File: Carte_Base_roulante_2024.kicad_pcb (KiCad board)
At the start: 2 copper layers, 62 x 80 mm, 69 parts, among them J11 ENCA, J4 ENCB, J5 ENCC, Q2 IRF7424, U1 STM32G484RETx

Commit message: Routage Terminé git status !
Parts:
- moved C2 0.19 mm to (213.2, 78.8)
- moved C4 0.19 mm to (213.2, 103.6)
- moved TP_GND1 0.13 mm to (177.3, 82.5)
- moved Transfo5->3.3 0.13 mm to (168.4, 127.2)
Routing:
- net GND: track 0.00 -> 120.9 mm, vias 0 -> 84
- net Net-(MOT2-Pin_1): track 0.00 -> 9.44 mm
- net /BOOT 0: track 16.5 -> 17.4 mm
- net IMU_INT1: track 7.10 -> 7.82 mm
- net +BATT: vias 9 -> 14
- added copper zone on B.Cu, net GND
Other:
- board size 62 x 80 mm -> 66 x 84 mm

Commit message: j'ai pas fait Ctrl S ...
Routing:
- net Enc2_B: track 23.0 -> 22.3 mm
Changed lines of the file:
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@@
   (segment (start 183.136 108.672) (end 183.136 109.757226) (width 0.3) (layer "F.Cu") (net 8))
   (segment (start 172.847 116.205) (end 176.022 113.03) (width 0.4) (layer "F.Cu") (net 8))
-  (segment (start 183.136 109.757226) (end 182.641613 110.251613) (width 0.3) (layer "F.Cu") (net 8))
   (segment (start 179.933938 113.03) (end 183.171356 109.792582) (width 0.4) (layer "F.Cu") (net 8))
   (segment (start 164.592 116.205) (end 172.847 116.205) (width 0.4) (layer "F.Cu") (net 8))
@@
   (segment (start 181.4025 93.7725) (end 180.34 93.7725) (width 0.3) (layer "B.Cu") (net 26))
   (segment (start 184.15 99.06) (end 183.515 98.425) (width 0.3) (layer "B.Cu") (net 26))
-  (segment (start 184.136 95.728182) (end 184.136 95.885) (width 0.3) (layer "F.Cu") (net 27))
-  (segment (start 184.136 95.885) (end 184.136 97.322) (width 0.3) (layer "F.Cu") (net 27))
   (segment (start 184.136 94.601) (end 184.134 94.599) (width 0.3) (layer "F.Cu") (net 27))
   (segment (start 183.408 94.572) (end 184.086 95.25) (width 0.4) (layer "F.Cu") (net 27))
-  (segment (start 184.136 94.601) (end 184.136 95.885) (width 0.3) (layer "F.Cu") (net 27))
+  (segment (start 184.136 95.3) (end 184.136 97.322) (width 0.3) (layer "F.Cu") (net 27))
+  (segment (start 184.136 95.2) (end 184.086 95.25) (width 0.3) (layer "F.Cu") (net 27))
+  (segment (start 184.136 94.601) (end 184.136 95.2) (width 0.3) (layer "F.Cu") (net 27))
   (segment (start 177.757 94.572) (end 183.408 94.572) (width 0.4) (layer "F.Cu") (net 27))
   (segment (start 184.134 94.599) (end 184.134 93.171144) (width 0.3) (layer "F.Cu") (net 27))
+  (segment (start 184.086 95.25) (end 184.136 95.3) (width 0.3) (layer "F.Cu") (net 27))
   (segment (start 184.134 92.7375) (end 184.134 93.171144) (width 0.25) (layer "F.Cu") (net 27))
   (segment (start 175.26 92.075) (end 177.757 94.572) (width 0.4) (layer "F.Cu") (net 27))

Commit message: Marquage
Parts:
- moved D3 1.02 mm to (186.6, 62.2)
- renumbered C12 to Ce, J11 to ENC_A1, J4 to ENC_B1, J5 to ENC_C1
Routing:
- net GND: track 120.9 -> 124.5 mm
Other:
- board text added: "+18"
- board text added: "100nF"
- board text added: "3x10uF"
- board text added: "BOOT"
- board text added: "ENC A"
- board text added: "ENC B"
- board text added: "ENC C"
- board text added: "GND"
- board text added: "LED"
- board text added: "R10k"
- board text added: "SONDE"
- board text added: "UART"
- board text added: "Zener"

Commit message: Carte terminé git status!
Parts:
- ENC_1: renamed from ENC_A1; value ENCA -> ENC1
- ENC_2: renamed from ENC_B1; value ENCB -> ENC2
- ENC_3: renamed from ENC_C1; value ENCC -> ENC3
- moved ENC_1 12.7 mm to (157.0, 116.2)
- moved ENC_2 12.7 mm to (157.0, 103.5)
- renumbered Ce to C12
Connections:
- U1 pad 12: Enc1_B -> Enc2_B
- U1 pad 13: Enc1_A -> Enc2_A
- U1 pad 20: Enc2_A -> Enc1_A
- U1 pad 21: Enc2_B -> Enc1_B
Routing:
- net Enc2_B: track 22.3 -> 16.7 mm
- net Enc1_B: track 16.7 -> 22.3 mm
- net Enc2_A: track 24.2 -> 20.1 mm
- net Enc1_A: track 20.1 -> 24.2 mm
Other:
- board text added: "CS"
- board text added: "MISO"
- board text added: "MOSI"
- board text added: "SCK"
- board text added: "SW"
- board text removed: "100nF"
- board text removed: "3x10uF"
- board text removed: "ENC A"
- board text removed: "ENC B"
- board text removed: "ENC C"
- board text removed: "R10k"
- board text removed: "SONDE"
- board text removed: "Zener"

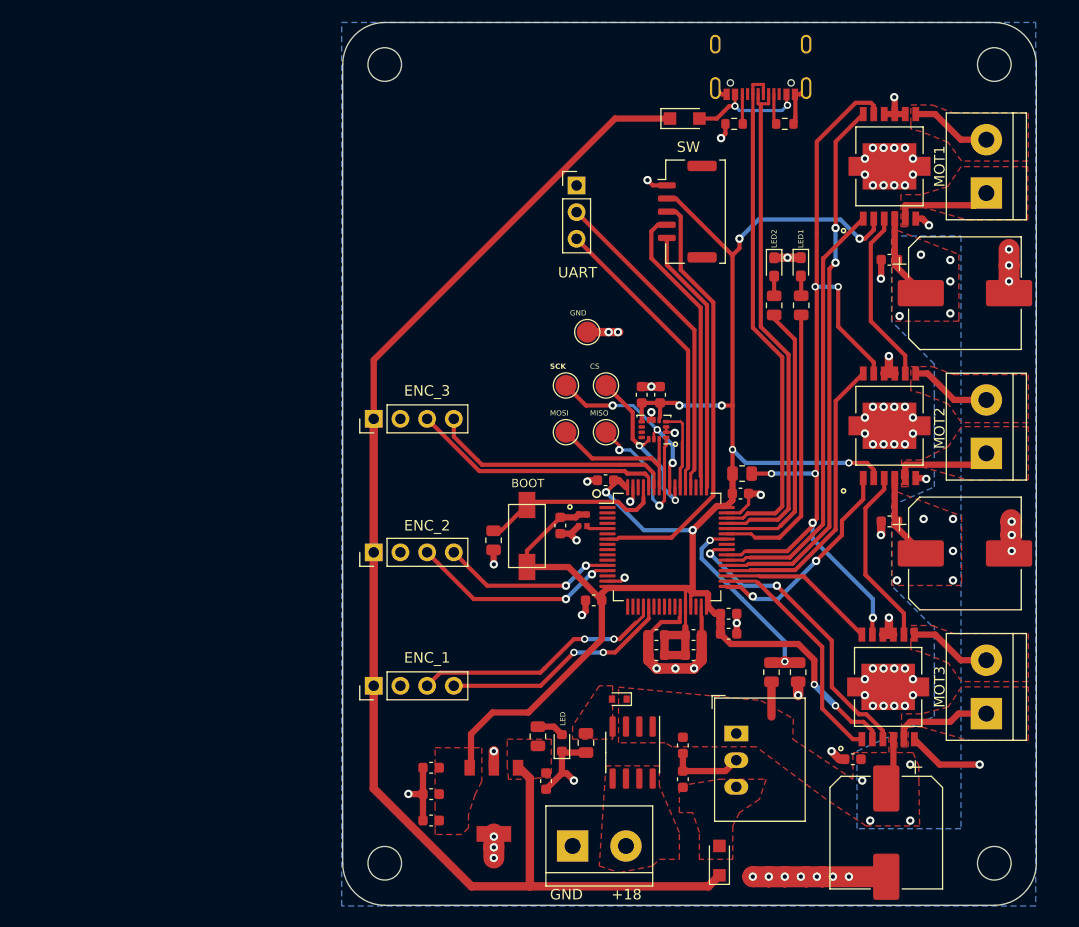
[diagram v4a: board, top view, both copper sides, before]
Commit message: ajuste espacement trous
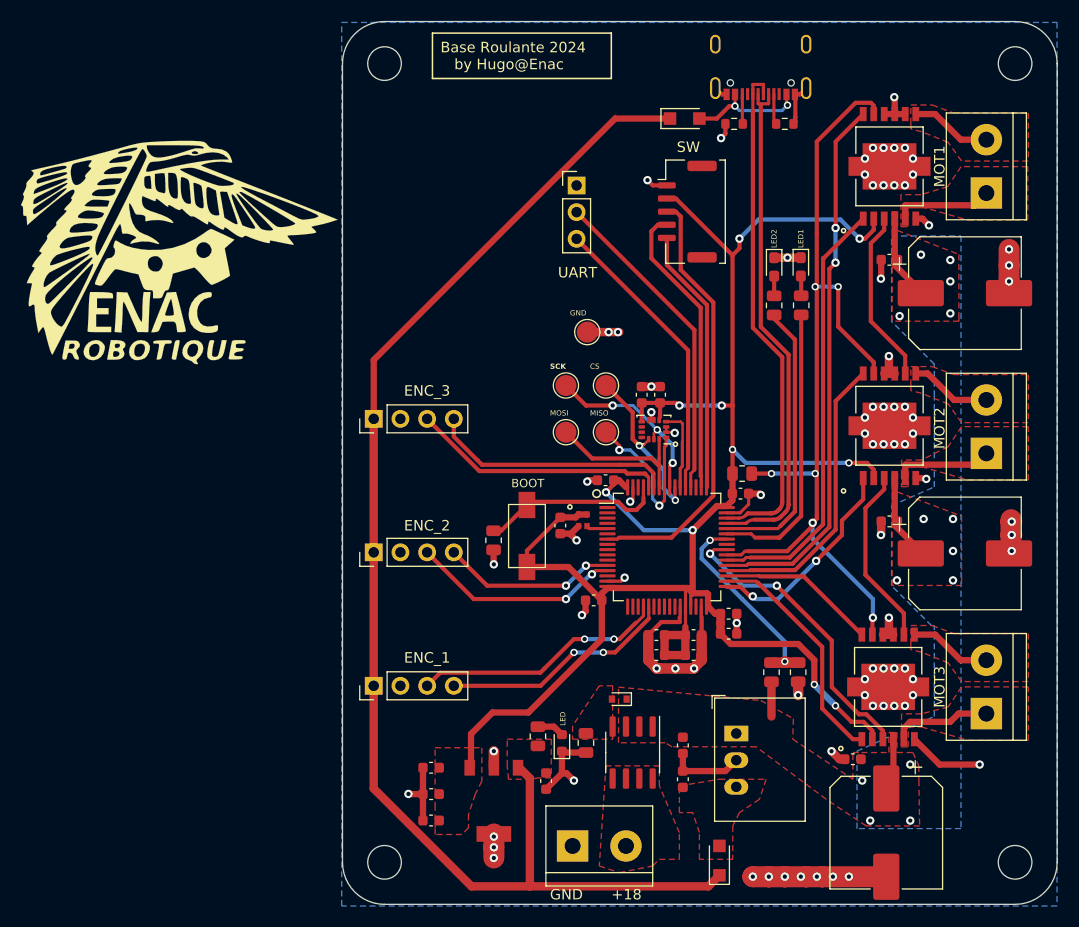
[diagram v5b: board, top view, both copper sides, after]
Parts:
- added G***: LOGO, library:logo, F.Cu at (138.4, 74.9)
- added G***: LOGO, library:logo, B.Cu at (133.6, 49.3)
- moved H2 1.98 mm to (218.0, 57.0)
- moved H3 1.98 mm to (218.0, 133.0)
- moved H1 0.09 mm to (158.0, 57.0)
- moved H4 0.09 mm to (158.0, 133.0)
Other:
- board size 66 x 84 mm -> 68 x 84 mm
- board text added: "Base Roulante 2024 by Hugo@Enac"

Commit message: corrections + courbe + stencil
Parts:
- removed the G*** at (138.4, 74.9)
- added G***: LOGO, ENAC_robotique:logo_enac_mini, F.Cu at (109.3, 121.3)
- added REF**: trou_stencil, ENAC_robotique:trou_stencil, F.Cu at (73.2, 71.0)
- added REF**: trou_stencil, ENAC_robotique:trou_stencil, F.Cu at (73.2, 131.0)
- ENC 1: renamed from ENC_1
- ENC 2: renamed from ENC_2
- ENC 3: renamed from ENC_3
- moved H2 115.6 mm to (103.2, 71.0), turned to 90 degrees
- moved USB-C1 100.7 mm to (101.4, 95.2), turned to -90 degrees
- moved MOT1 99.8 mm to (115.6, 73.7), turned to 180 degrees
- moved U6 94.4 mm to (113.0, 83.0), turned to 180 degrees
- moved R7 92.2 mm to (109.0, 92.9), turned to 90 degrees
- moved H1 92.1 mm to (103.2, 131.0), turned to 90 degrees
- moved R8 89.4 mm to (109.0, 97.7), turned to -90 degrees
- moved C2 88.2 mm to (125.1, 75.8), turned to 90 degrees
- moved D3 87.8 mm to (108.5, 102.4), turned to 90 degrees
- moved C1 84.4 mm to (121.9, 83.0), turned to -90 degrees
- moved MOT2 77.6 mm to (140.3, 73.7), turned to 180 degrees
- moved LED1 76.5 mm to (122.6, 91.4), turned to 0 degrees
- moved DEBUG1 76.1 mm to (117.3, 102.2), turned to 0 degrees
- moved UART4 75.6 mm to (114.8, 112.7), turned to 90 degrees
- moved LED2 74.6 mm to (122.6, 93.9), turned to 0 degrees
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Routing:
- net +3.3V: track 189.9 -> 188.0 mm
- net Net-(MOT2-Pin_1): track 9.44 -> 10.9 mm
- net GND: track 124.6 -> 123.8 mm
- net DIS: track 85.1 -> 84.5 mm
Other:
- board size 68 x 84 mm -> 84 x 68 mm
- board text added: "A"
- board text added: "B"

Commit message: correctif
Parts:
- removed the G*** at (109.3, 121.3)
- added G***: LOGO, ENAC_robotique:logo_enac_moyen, F.Cu at (219.2, 62.2)
- moved H2 167.8 mm to (270.0, 52.8), turned to 0 degrees
- moved locked 152.0 mm to (267.3, 65.1), turned to 90 degrees
- moved USB-C1 151.0 mm to (245.8, 50.9), turned to 180 degrees
- moved U6 146.5 mm to (258.1, 62.6), turned to 90 degrees
- moved R7 143.3 mm to (248.1, 58.5), turned to 0 degrees
- moved C2 140.1 mm to (265.2, 74.8), turned to 0 degrees
- moved R8 139.9 mm to (243.3, 58.5), turned to 180 degrees
- moved D3 137.5 mm to (238.6, 58.0), turned to 0 degrees
- moved C1 136.7 mm to (258.0, 70.5), turned to 180 degrees
- moved H1 132.4 mm to (210.0, 52.8), turned to 0 degrees
- moved LED1 128.5 mm to (249.6, 72.1), turned to -90 degrees
- moved locked 128.0 mm to (267.3, 89.9), turned to 90 degrees
- moved DEBUG1 126.5 mm to (238.8, 66.9), turned to -90 degrees
- moved LED2 126.4 mm to (247.1, 72.1), turned to -90 degrees
- moved R10 124.4 mm to (249.7, 75.8), turned to 90 degrees
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- renumbered MOT3 to locked, MOT2 to locked, MOT1 to locked
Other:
- board size 84 x 68 mm -> 68 x 84 mm
- board text added: "BOOT0"
- board text added: "JLCJLCJLCJLC"
- board text added: "MOT 1"
- board text added: "MOT 2"
- board text added: "MOT 3"
- board text removed: "BOOT"

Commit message: fix DRC
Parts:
- removed REF** (x2): trou_stencil, ENAC_robotique:trou_stencil
- moved DEBUG1 119.9 mm to (119.8, 81.1)
- moved LED1 119.9 mm to (130.6, 86.3)
- moved R10 119.9 mm to (130.6, 90.0)
- moved R7 119.9 mm to (129.1, 72.7)
- moved TP_CS1 119.9 mm to (112.1, 97.6)
- moved TP_MISO1 119.9 mm to (112.1, 102.1)
- moved U2 119.9 mm to (139.0, 101.5)
- moved U3 119.9 mm to (138.9, 126.3)
- moved U6 119.9 mm to (139.0, 76.8)
- moved ALIM1 119.9 mm to (108.9, 141.4)
- moved C11 119.9 mm to (123.7, 121.3)
- moved C16 119.9 mm to (115.5, 98.5)
- moved C23 119.9 mm to (119.4, 131.9)
- moved C24 119.9 mm to (119.4, 135.1)
- moved C7 119.9 mm to (110.9, 118.1)
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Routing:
- net GND: track 123.8 -> 201.7 mm, vias 84 -> 70
- net Net-(D2-A): track 0.00 -> 11.4 mm
- net +3.3V: track 188.0 -> 196.4 mm
- net +5V: track 127.1 -> 132.1 mm
- net Enc1_A: track 24.0 -> 25.4 mm
- net ERROR_FLAG: track 28.1 -> 28.7 mm
- removed copper zone on F.Cu, net +3.3V
- removed copper zone on F.Cu, net +5V
- removed copper zone on F.Cu, net Net-(D2-A)
